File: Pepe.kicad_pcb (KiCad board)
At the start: 2 copper layers, 35.6 x 43.2 mm, 10 parts, among them P1 USB_OTG, P2 VOC_CONN, P3 DBG_SETPOINT, P4 DBG_VOC, P5 DBG_OUTPUT, U1 MIC7211YM5, U2 APT7335A-50

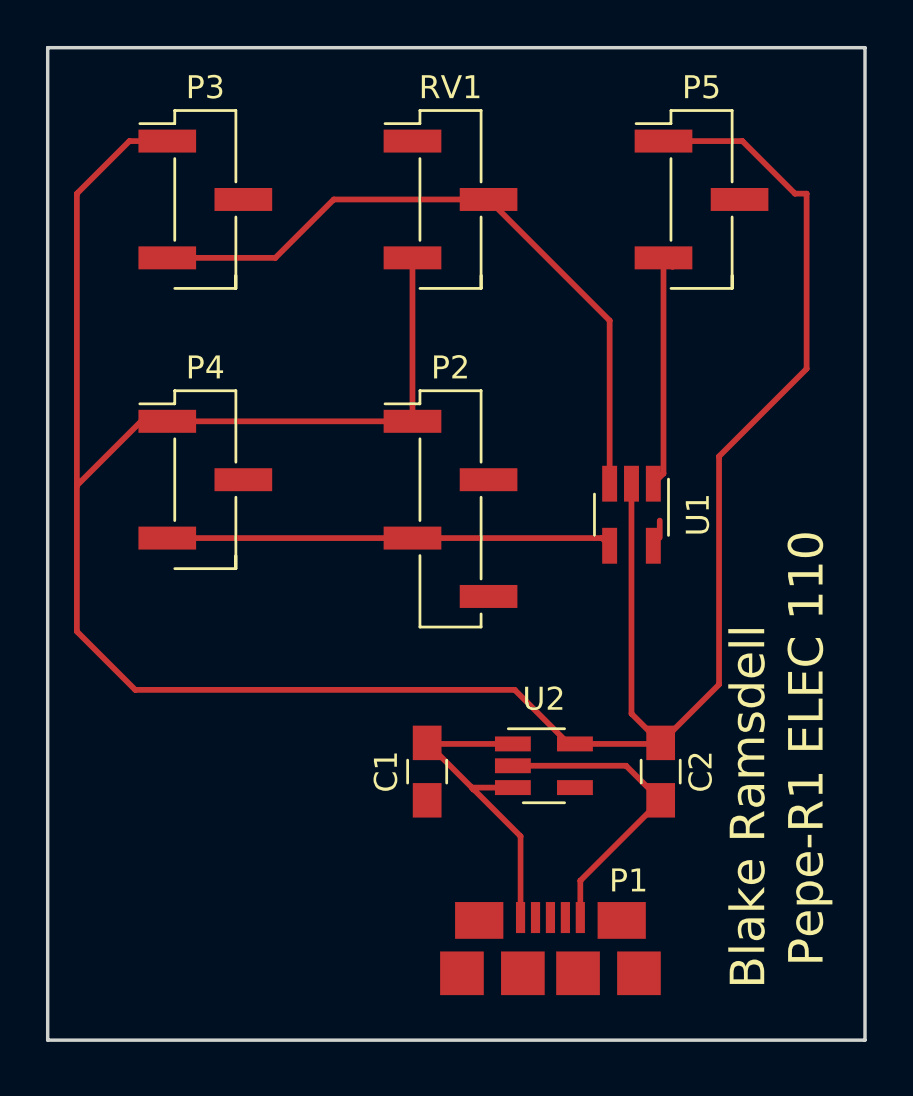
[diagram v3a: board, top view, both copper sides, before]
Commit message: Added LEDs.
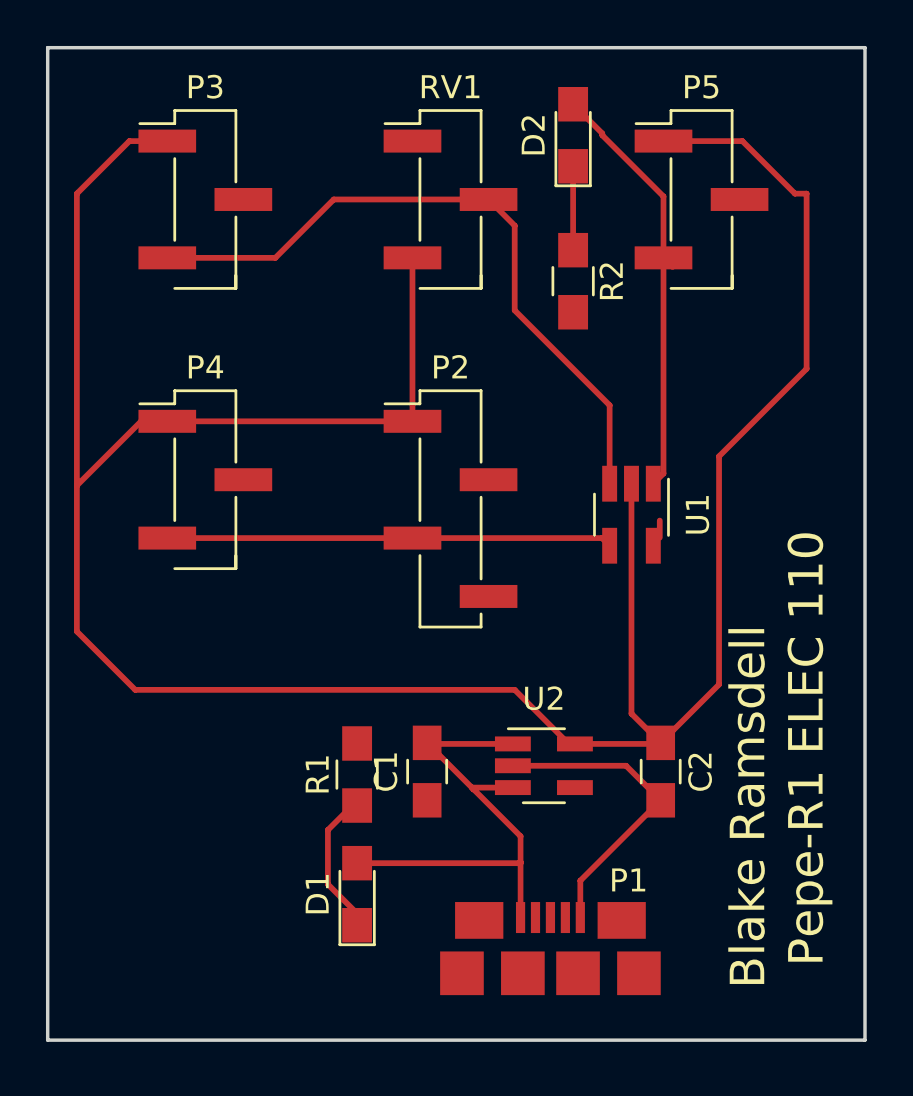
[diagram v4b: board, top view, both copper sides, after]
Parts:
- added D1: GREEN, LEDs:LED_0805_HandSoldering, F.Cu at (79.5, 77.5)
- added D2: RED, LEDs:LED_0805_HandSoldering, F.Cu at (88.9, 44.5)
- added R1: 150 Ω, Resistors_SMD:R_0805_HandSoldering, F.Cu at (79.5, 72.3)
- added R2: 150 Ω, Resistors_SMD:R_0805_HandSoldering, F.Cu at (88.9, 50.8)
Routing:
- net OUTPUT: track 10.6 -> 18.9 mm
- net Net-(D1-Pad1): track 0.00 -> 7.10 mm
- net VCC: track 14.8 -> 21.5 mm
- net Net-(D2-Pad1): track 0.00 -> 3.65 mm
